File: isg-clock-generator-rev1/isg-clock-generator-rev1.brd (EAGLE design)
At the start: 76.2 x 50.8 mm, 68 parts, among them IC1 LMK03318RHSR, X1 OUT0_P, X2 OUT0_N, X3 OUT1_P, X4 OUT1_N

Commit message: More progress idk
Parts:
- removed JP1: (no value), jumper:JP5Q
- added C44, C45, C49, C50: CAP CER 10000PF 25V X7R 0603 10%, rcl-modified-footprints:C0603
- added C46, C48, C51, C53: CAP CER 0.1UF 25V X7R 0603 10%, rcl-modified-footprints:C0603
- added C47, C52: CAP CER 10UF 16V X7R 0805 20%, rcl:C0805
- added C54: CAP CER 0.01uF X7R 0402, rcl-modified-footprints:C0402
- added C55: CAP CER 22uF 6.3V 0603, rcl-modified-footprints:C0603
- added C56: CAP CER 0.033uF 0603, rcl-modified-footprints:C0603
- added C57: CAP CER 3300pF 0603, rcl-modified-footprints:C0603
- added C58, C62, C63: DNP, rcl-modified-footprints:C0603
- added C59, C60: 0R JUMPER, rcl-modified-footprints:C0603
- added C61: DNP, rcl-modified-footprints:C0402
- added IC2, IC3: TPS7A4901, Kramnik's Library:MSOP-8_POWER_PAD
- added JP10: RSEL, isg-clock-generator:JP2_ROUND
- added JP11: (no value), jumper:JP8Q
- added JP12: (no value), jumper:JP3Q
- added JP13: PRIREF_VCM, jumper:JP2
- added JP14: CON_OST_302-S101, Kramnik's Library:CON_OST_302-S101
- added JP2: STAT_LED_EN, jumper:JP1
- added JP3: GPIO5, isg-clock-generator:JP2_ROUND
- added JP4: GPIO4, isg-clock-generator:JP2_ROUND
- added JP5: GPIO3, isg-clock-generator:JP2_ROUND
- added JP6: GPIO2, isg-clock-generator:JP2_ROUND
- added JP7: GPIO1, isg-clock-generator:JP2_ROUND
- added JP8: GPIO0, isg-clock-generator:JP2_ROUND
- added JP9: HWCTRL, isg-clock-generator:JP2_ROUND
- added R10, R14: RES SMD 76.8K OHM 1% 1/10W 0603, rcl-modified-footprints:R0603
- added R11, R12, R13, R26, R28, R29, R41, R42, R44, R45, R49, R50, R51, R52, R53, R6, R8, R9: DNP, rcl-modified-footprints:R0603
- added R15, R17, R18, R7: RES SMD 24K OHM 1% 1/10W 0603, rcl-modified-footprints:R0603
- added R16, R27, R30, R33, R36, R40, R43: RES SMD 1K OHM 1% 1/10W 0603, rcl-modified-footprints:R0603
- added R19: RES SMD 0 OHM 1% 1/10W 0603, rcl-modified-footprints:R0603
- added R20: RES SMD 2.32K OHM 1% 1/10W 0603, rcl-modified-footprints:R0603
- added R21: RES SMD 5.62K OHM 1% 1/10W 0603, rcl-modified-footprints:R0603
- added R22: RES SMD 10.5K OHM 1% 1/10W 0603, rcl-modified-footprints:R0603
- added R23: RES SMD 18.7K OHM 1% 1/10W 0603, rcl-modified-footprints:R0603
- added R24: RES SMD 34.8K OHM 1% 1/10W 0603, rcl-modified-footprints:R0603
- added R25: RES SMD 84.5K OHM 1% 1/10W 0603, rcl-modified-footprints:R0603
- added R3, R4, R46, R47, R48, R5: 0R JUMPER 0603, rcl-modified-footprints:R0603
- added R31, R34, R37, R39: RES SMD 13.0K OHM 1% 1/10W 0603, rcl-modified-footprints:R0603
- added R32, R35, R38: RES SMD 4.99K OHM 1% 1/10W 0603, rcl-modified-footprints:R0603
- added X5: OUT1_P, con-coax:J502-ND-142-0701-881/886
- Q1: value (none) -> 7M50072001
- R1, R2: value 510 -> RES SMD 510R 0603
- X3: value OUT1_P -> OUT2_P
- X4: value OUT1_N -> OUT1_P
- moved LED1 95.0 mm to (19.7, 43.8), turned to 270 degrees
- moved LED2 93.5 mm to (19.7, 40.3), turned to 270 degrees
- moved X4 89.4 mm to (47.6, 61.9), turned to 270 degrees
- moved X3 42.7 mm to (19.1, 1.59), turned to 90 degrees
- moved X2 40.9 mm to (38.1, 1.59), turned to 90 degrees
- moved X1 38.9 mm to (57.1, 1.59), turned to 90 degrees
- moved Q1 25.7 mm to (34.3, 44.5), turned to 270 degrees
- moved C7 13.1 mm to (29.2, 29.2), turned to 270 degrees
- moved C1 12.7 mm to (36.8, 35.6), turned to 90 degrees
- moved H3 12.7 mm to (72.4, 59.7)
- moved H4 12.7 mm to (3.81, 59.7)
- moved C2 5.24 mm to (47.0, 27.9)
- moved C3 5.24 mm to (47.0, 24.1)
- moved IC1 2.84 mm to (38.1, 25.4)
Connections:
- net LF2 renamed NC_PIN
- net N$17 renamed STATUS0
- net N$18 renamed STATUS1
- removed net N$15: IC1.10
- removed net N$16: IC1.7
- removed net N$19: IC1.6
- removed net NC_OUT2_P: IC1.20
- removed net OUT1_N: IC1.16, X4.1
- removed net OUT1_P: IC1.17, X3.1
- new net GPIO5_SEL_11_12: JP11.12, R24.2
- new net GPIO5_SEL_13_14: JP11.14, R25.2
- new net GPIO5_SEL_15_16: JP11.16, R26.2
- new net GPIO5_SEL_1_2: JP11.2, R19.2
- new net GPIO5_SEL_3_4: JP11.4, R20.2
- new net GPIO5_SEL_5_6: JP11.6, R21.2
- new net GPIO5_SEL_7_8: JP11.8, R22.2
- new net GPIO5_SEL_9_10: JP11.10, R23.2
- new net LDO_P3V3_SS: C44.1, C49.1, IC2.6, IC3.6
- new net LDO_P5V0_FB_CH1: C45.2, C50.2, IC2.2, IC3.2, R10.1, R14.1, R15.1, R7.1
- new net N$1: R6.2, R8.2, R9.2
- new net N$10: JP14.3
- new net N$11: JP14.1
- new net N$12: JP14.8
- new net N$13: JP14.4
- new net N$22: C55.1, JP12.5
- new net N$23: C56.1, JP12.3
- new net N$24: JP4.2, R27.1
- new net N$25: JP5.2, R30.1
- new net N$26: JP8.2, R39.1
- new net N$27: JP6.2, R33.1
- new net N$28: JP9.2, R40.1
- new net N$29: JP7.2, R36.1
- new net N$30: C57.1, JP12.1
- new net N$31: JP10.2, R43.1
- new net N$32: JP12.2, JP12.4, JP12.6, R46.2
- new net N$4: JP3.3, R16.1
- new net N$5: JP13.3, R51.1, R52.2
- new net N$6: JP14.5, R53.1
- new net NC_OUT1_N: IC1.16
- new net NC_OUT1_P: IC1.17
- new net OUT0_R_N: R12.2, R4.1, R8.1, X2.1
- new net OUT0_R_P: R11.2, R3.1, R6.1, X1.1
- new net OUT2_P: IC1.20, R5.2
- new net OUT2_R_P: R13.2, R5.1, R9.1, X3.1
- new net PP_P1V8_VDDO: C26.1, C30.1, C34.1, C38.1, C42.1, C45.1, C46.1, C47.1, C6.1, IC2.1, L1.2, L10.2, L6.2, L7.2, L8.2, L9.2, R10.2
- new net PP_P3V3_PLL_CORE: C20.1, C21.1, C22.1, C23.1, C50.1, C51.1, C52.1, IC3.1, JP10.3, JP2.2, JP4.3, JP5.3, JP6.3, JP7.3, JP8.3, JP9.3, L2.1, L3.1, L4.1, L5.1, R14.2, R16.2, R17.1, R28.2, R31.2, R34.2, R37.2, R41.2, R44.2, R51.2, R53.2
- new net PRIREF_N: IC1.7, R48.1, R50.2
- new net PRIREF_P: IC1.6, R47.1, R49.2
- new net PRIREF_RC_N: C60.1, X5.1
- new net PRIREF_RC_P: C59.1, X4.1
- new net PRIREF_R_N: C60.2, R48.2
- new net PRIREF_R_P: C59.2, R47.2
- new net PRIREF_VCM: C61.1, JP13.2, R49.1, R50.1
- new net SECREF_N: C62.1, IC1.11, Q1.1
- new net SECREF_P: C63.1, IC1.10, Q1.3
- new net STATUS_LED_PWR: JP2.1, R1.2, R2.2
- new net VIN: C48.1, C53.1, IC2.8, IC3.8, R18.1
- net GND: now also C44.2, C46.2, C47.2, C48.2, C49.2, C51.2, C52.2, C53.2, C54.2, C55.2, C56.2, C57.2, C58.2, C61.2, C62.2, C63.2, IC2.4, IC2.PAD, IC3.4, IC3.PAD, JP10.1, JP11.1, JP11.11, JP11.13, JP11.15, JP11.3, JP11.5, JP11.7, JP11.9, JP13.1, JP14.6, JP3.1, JP4.1, JP5.1, JP6.1, JP7.1, JP8.1, JP9.1, R11.1, R12.1, R13.1, R15.2, R29.1, R32.1, R35.1, R38.1, R42.1, R45.1, R52.1, R7.2, X5.G@1, X5.G@2, X5.G@3, X5.G@4
- net GPIO0: now also R39.2
- net GPIO1: now also R36.2, R37.1, R38.2
- net GPIO2: now also R33.2, R34.1, R35.2
- net GPIO3: now also R30.2, R31.1, R32.2
- net GPIO4: now also R27.2, R28.1, R29.2
- net GPIO5: now also JP3.2, R19.1, R20.1, R21.1, R22.1, R23.1, R24.1, R25.1, R26.1
- net HW_SW_CTRL: now also R40.2, R41.1, R42.2
- net LF1: now also C58.1, R46.1
- net N$14: now also JP14.2; no longer IC1.11
- net N$2: now also IC2.5, R17.2; no longer C20.1, C21.1, C22.1, C23.1, L2.1, L3.1, L4.1, L5.1
- net N$3: now also IC3.5, R18.2; no longer C26.1, C30.1, C34.1, C38.1, C42.1, C6.1, L1.2, L10.2, L6.2, L7.2, L8.2, L9.2
- net N$9: now also JP14.7; no longer R1.2, R2.2
- net OUT0_N: now also R4.2; no longer X2.1
- net OUT0_P: now also R3.2; no longer X1.1
- net PDN: now also C54.1
- net REFSEL: now also R43.2, R44.1, R45.2
- net SCL: now also JP14.9
- net SDA: now also JP14.10
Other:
- board size 76.2 x 50.8 mm -> 76.2 x 63.5 mm
- board text added: "1GHz PLL Clock Source kramnik@berkeley.edu"

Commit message: Started decap placement
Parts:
- IC1: device isg-clock-generator:RHS0048A -> isg-clock-generator:RHS0048A_NV
- X4: value OUT1_P -> PRIREF_P
- X5: value OUT1_P -> PRIREF_N
- moved C40 302.4 mm to (39.1, 17.5), turned to 270 degrees
- moved C43 299.6 mm to (39.1, 19.7), turned to 270 degrees
- moved C41 296.1 mm to (39.1, 21.3), flipped to the bottom, turned to 90 degrees
- moved C36 293.3 mm to (41.0, 33.3), turned to 90 degrees
- moved C39 286.1 mm to (41.0, 31.1), turned to 90 degrees
- moved C37 279.6 mm to (41.0, 29.5), flipped to the bottom, turned to 270 degrees
- moved C32 268.1 mm to (39.4, 33.3), turned to 90 degrees
- moved C35 260.9 mm to (39.4, 31.1), turned to 90 degrees
- moved C33 254.4 mm to (39.4, 29.5), flipped to the bottom, turned to 270 degrees
- moved C28 242.8 mm to (37.8, 33.3), turned to 90 degrees
- moved C31 235.7 mm to (37.8, 31.1), turned to 90 degrees
- moved C29 229.2 mm to (37.8, 29.5), flipped to the bottom, turned to 270 degrees
- moved C24 217.7 mm to (36.2, 33.3), turned to 90 degrees
- moved C27 210.6 mm to (36.2, 31.1), turned to 90 degrees
- moved C25 204.1 mm to (36.2, 29.5), flipped to the bottom, turned to 270 degrees
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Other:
- board text added: "1GHz PLL Clock Source kramnik@berkeley.edu vlada@berkeley.edu"
- board text removed: "1GHz PLL Clock Source kramnik@berkeley.edu"

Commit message: Fit all components on board except power supplies (need to swap LDO part)
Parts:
- JP13: device jumper:JP2 -> isg-clock-generator:JP2_ROUND
- moved C52 437.5 mm to (52.4, 99.4)
- moved R52 424.4 mm to (23.8, 60.0)
- moved R53 419.6 mm to (5.40, 56.2)
- moved R51 419.2 mm to (20.6, 60.0)
- moved R12 338.9 mm to (54.6, 8.57)
- moved R13 338.2 mm to (16.2, 9.21)
- moved R11 331.1 mm to (35.2, 8.57), turned to 180 degrees
- moved R8 327.2 mm to (59.4, 8.89)
- moved R9 325.2 mm to (21.6, 8.89)
- moved R6 318.4 mm to (40.0, 8.26)
- moved C38 303.3 mm to (41.0, 38.4), turned to 90 degrees
- moved C42 302.4 mm to (39.1, 12.4), turned to 270 degrees
- moved L10 284.9 mm to (39.1, 14.9), turned to 270 degrees
- moved L9 280.8 mm to (41.0, 35.9), turned to 90 degrees
- moved C34 278.0 mm to (39.4, 38.4), turned to 90 degrees
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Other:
- board size 76.2 x 63.5 mm -> 76.2 x 76.2 mm

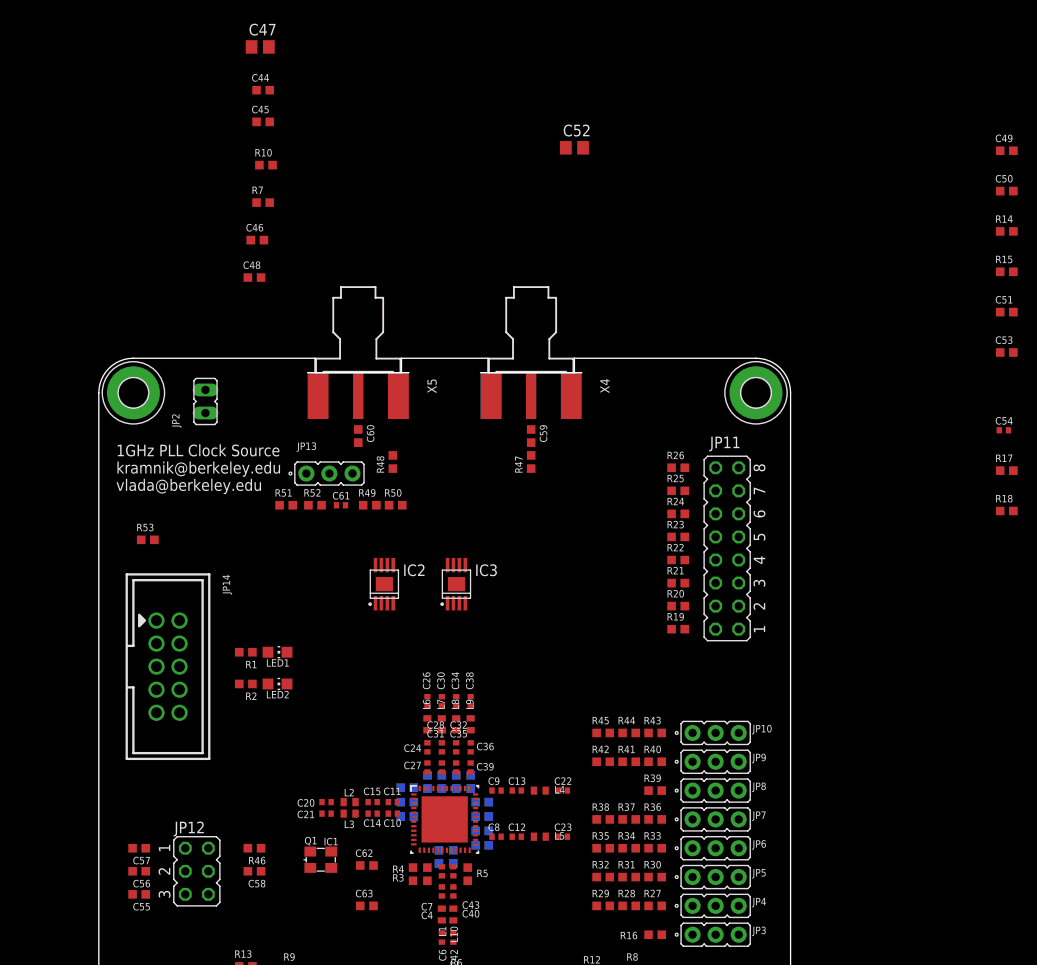
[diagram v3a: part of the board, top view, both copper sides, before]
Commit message: Updated LDOs for 1A, all parts roughly placed in layout, power input TODO
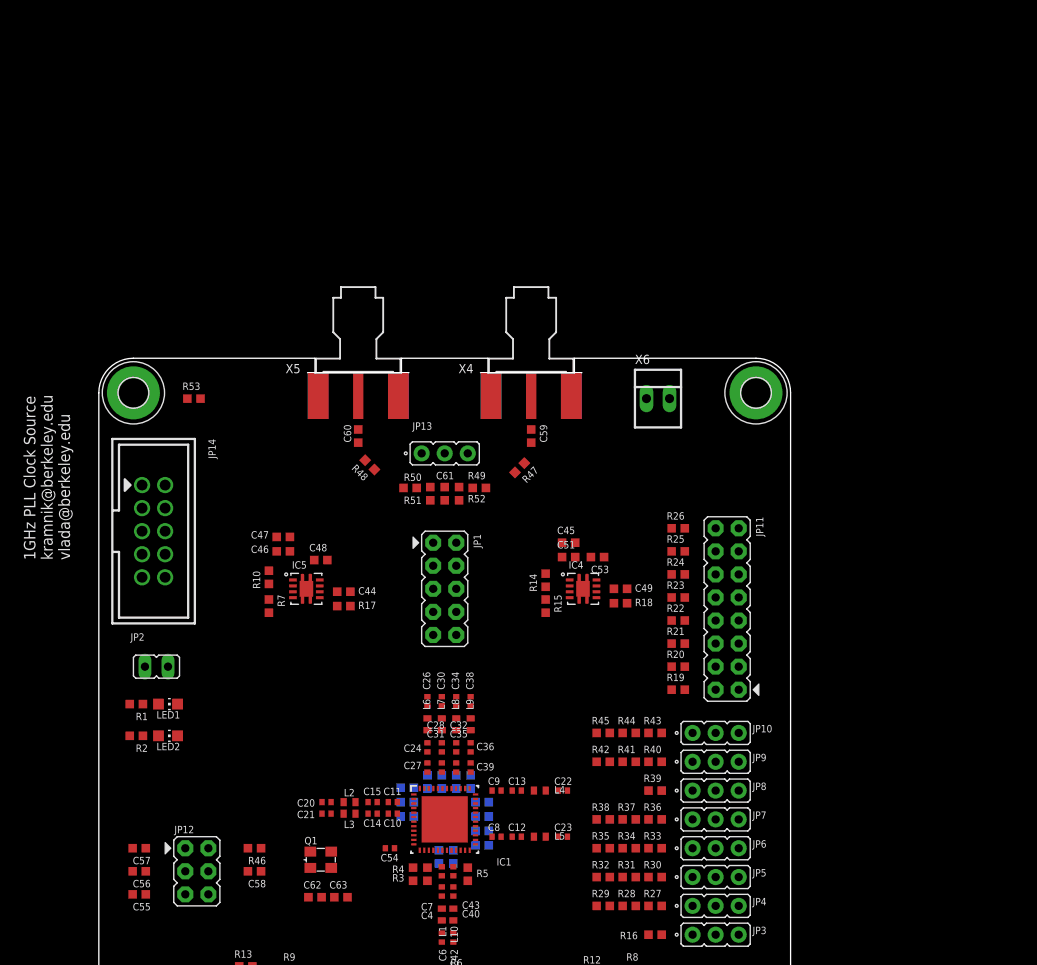
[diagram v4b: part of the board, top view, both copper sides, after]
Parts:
- removed C50: CAP CER 10000PF 25V X7R 0603 10%, rcl-modified-footprints:C0603
- removed C52: CAP CER 10UF 16V X7R 0805 20%, rcl:C0805
- removed IC2, IC3: TPS7A4901, Kramnik's Library:MSOP-8_POWER_PAD
- added IC4, IC5: TPS7A8001DRBR, isg-clock-generator:DRB8_1P75X1P5
- added JP1: MOTHERBOARD, isg-clock-generator:JP5Q
- added X6: 22-23-2021, con-molex:22-23-2021
- C45: value CAP CER 10000PF 25V X7R 0603 10% -> CAP CER 4.7UF 6.3V X5R 0603 10%
- C47: value CAP CER 10UF 16V X7R 0805 20% -> CAP CER 4.7UF 6.3V X5R 0603 10%; device rcl:C0805 -> rcl-modified-footprints:C0603
- C61: value DNP -> DNP 0603; device rcl-modified-footprints:C0402 -> rcl-modified-footprints:C0603
- JP11: value (none) -> XO_MARGIN; device jumper:JP8Q -> isg-clock-generator:JP8Q
- JP12: value (none) -> LOOP_FILTER; device jumper:JP3Q -> isg-clock-generator:JP3Q
- R10, R14: value RES SMD 76.8K OHM 1% 1/10W 0603 -> RES SMD 4.99K OHM 1% 1/10W 0603
- R15: value RES SMD 24K OHM 1% 1/10W 0603 -> RES SMD 1.62K OHM 1% 1/10W 0603
- R17, R18: value RES SMD 24K OHM 1% 1/10W 0603 -> RES SMD 4.99K OHM 1% 1/10W 0603
- R51, R52: value DNP -> DNP 0603
- R7: value RES SMD 24K OHM 1% 1/10W 0603 -> RES SMD 3.92K OHM 1% 1/10W 0603
- moved C54 81.8 mm to (32.1, 22.2), turned to 180 degrees
- moved R17 74.5 mm to (27.0, 48.9), turned to 180 degrees
- moved C49 64.3 mm to (57.5, 50.8)
- moved R14 63.7 mm to (49.2, 51.8), turned to 90 degrees
- moved R15 62.7 mm to (49.2, 48.9), turned to 270 degrees
- moved C45 57.3 mm to (51.8, 55.9)
- moved C44 56.0 mm to (27.0, 50.5)
- moved C51 55.3 mm to (51.8, 54.3)
- moved C47 54.0 mm to (20.3, 56.5)
- moved C53 50.4 mm to (54.9, 54.3), turned to 180 degrees
- moved R10 45.4 mm to (18.7, 52.1), turned to 90 degrees
- moved R7 44.5 mm to (18.7, 48.9), turned to 270 degrees
- moved R18 43.7 mm to (57.5, 49.2), turned to 180 degrees
- moved C46 34.4 mm to (20.3, 54.9)
- moved C48 32.0 mm to (24.4, 54.0)
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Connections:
- net N$22 renamed LF_NARROW
- net N$23 renamed LF_FRAC_N
- net N$30 renamed LF_INT_N\
- net N$32 renamed LF_R
- removed net LDO_P3V3_SS: C44.1, C49.1, IC2.6, IC3.6
- removed net LDO_P5V0_FB_CH1: C45.2, C50.2, IC2.2, IC3.2, R10.1, R14.1, R15.1, R7.1
- removed net N$2: IC2.5, R17.2
- removed net N$3: IC3.5, R18.2
- new net LDO_PVCORE_EN: IC4.5, R18.2
- new net LDO_PVCORE_FB: IC4.3, R14.1, R15.1
- new net LDO_PVCORE_SS: C49.1, IC4.6
- new net LDO_PVDDIO_EN: IC5.5, R17.2
- new net LDO_PVDDIO_FB: IC5.3, R10.1, R7.1
- new net LDO_PVDDIO_SS: C44.1, IC5.6
- net GND: now also C45.2, IC4.4, IC4.9, IC5.4, IC5.9; no longer C52.2, IC2.4, IC2.PAD, IC3.4, IC3.PAD
- net PP_P1V8_VDDO: now also IC5.1, IC5.2; no longer C45.1, IC2.1
- net PP_P3V3_PLL_CORE: now also C45.1, IC4.1, IC4.2; no longer C50.1, C52.1, IC3.1
- net VIN: now also IC4.7, IC4.8, IC5.7, IC5.8; no longer IC2.8, IC3.8
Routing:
- added copper zone on layer 2, net GND

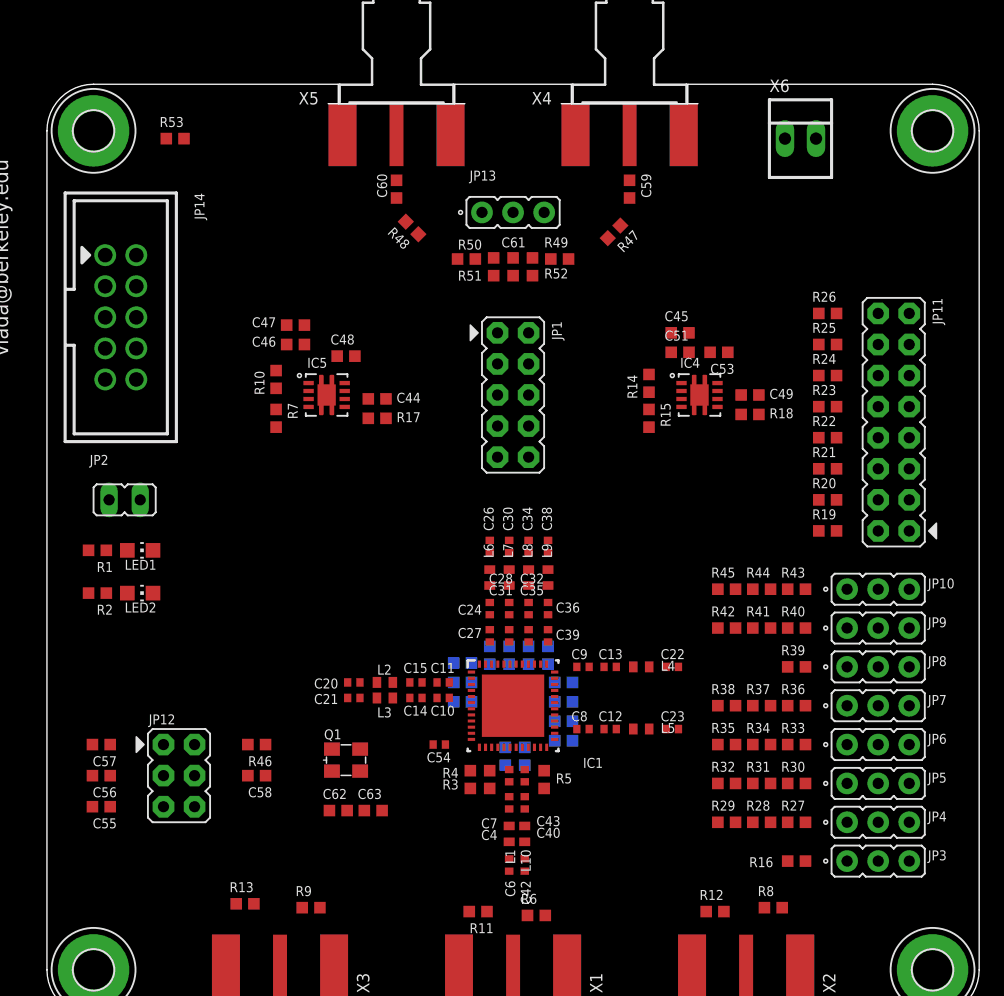
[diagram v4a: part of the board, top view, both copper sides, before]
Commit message: Started working on routing
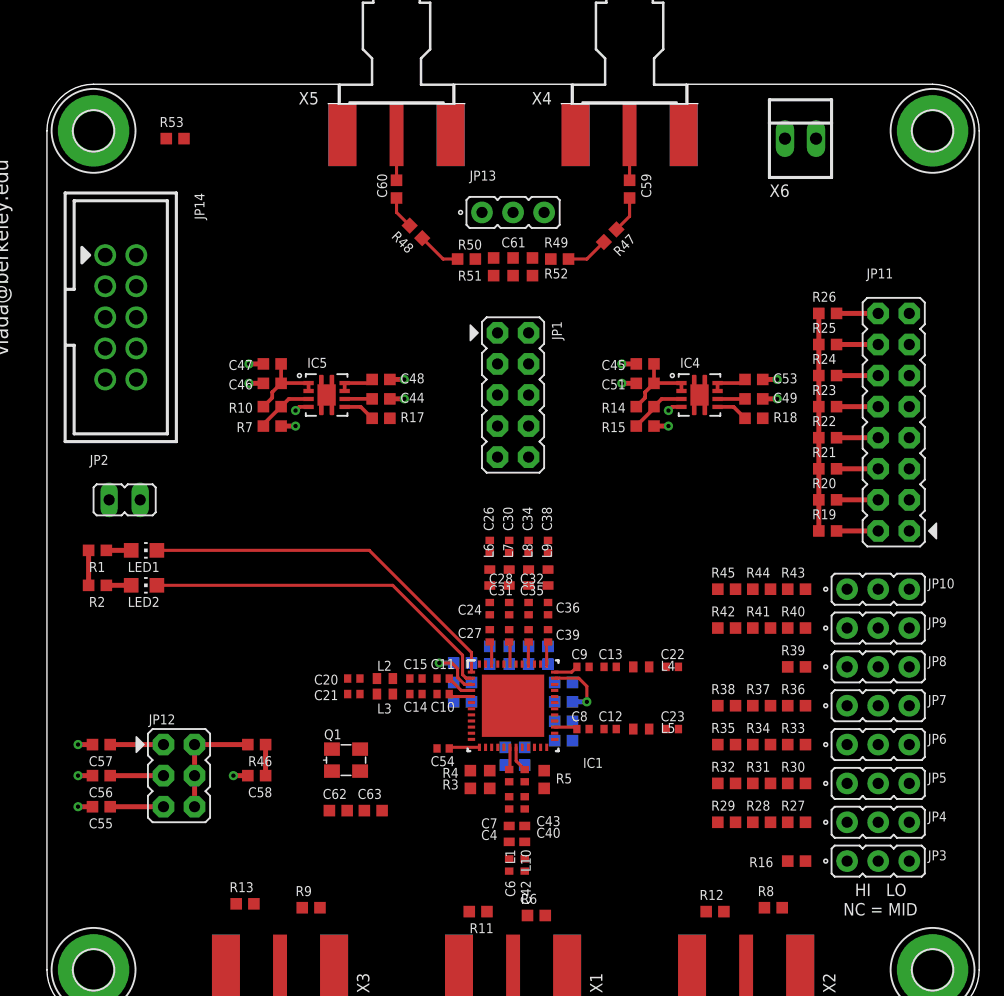
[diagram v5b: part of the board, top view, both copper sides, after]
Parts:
- JP10: value RSEL -> REFSEL
- R40: value RES SMD 1K OHM 1% 1/10W 0603 -> RES SMD 10K OHM 1% 1/10W 0603
- X6: value 22-23-2021 -> V_INPUT
- moved C45 3.82 mm to (48.9, 53.3), turned to 180 degrees
- moved C51 3.82 mm to (48.9, 51.8), turned to 180 degrees
- moved C46 3.70 mm to (18.4, 51.8), turned to 180 degrees
- moved C47 3.70 mm to (18.4, 53.3), turned to 180 degrees
- moved C53 3.62 mm to (57.8, 52.1), turned to 0 degrees
- moved C48 3.43 mm to (27.3, 52.1)
- moved R10 2.25 mm to (18.4, 49.8), turned to 180 degrees
- moved R14 1.93 mm to (48.9, 49.8), turned to 180 degrees
- moved R7 0.71 mm to (18.4, 48.3), turned to 0 degrees
- moved R15 0.71 mm to (48.9, 48.3), turned to 0 degrees
- moved LED2 0.71 mm to (7.94, 35.2)
- moved R2 0.63 mm to (4.13, 35.2)
- moved C54 0.45 mm to (32.4, 21.9)
- moved R47 0.45 mm to (46.0, 63.8)
- moved R48 0.45 mm to (30.2, 64.1)
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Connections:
- net GND: now also JP1.3, JP1.4, JP1.6
- net HW_SW_CTRL: now also JP1.8
- net SCL: now also JP1.10
- net SDA: now also JP1.9
- net STATUS0: now also JP1.7
- net STATUS1: now also JP1.5
- net VIN: now also JP1.1, JP1.2
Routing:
- net STATUS0: track 0.00 -> 30.8 mm
- net STATUS1: track 0.00 -> 29.8 mm
- net GND: track 0.00 -> 18.9 mm, vias 0 -> 16
- net GPIO5: track 0.00 -> 17.8 mm
- net LF_R: track 0.00 -> 9.44 mm
- net PP_P1V8_VDDO: track 0.00 -> 7.00 mm
- net PP_P3V3_PLL_CORE: track 0.00 -> 6.98 mm
- net VIN: track 0.00 -> 6.03 mm
- net DECAP_PLL: track 0.00 -> 5.36 mm, vias 0 -> 1
- net DECAP_DIG: track 0.00 -> 4.95 mm, vias 0 -> 1
- net LDO_PVDDIO_FB: track 0.00 -> 4.69 mm
- net LDO_PVCORE_FB: track 0.00 -> 4.69 mm
- net LF_NARROW: track 0.00 -> 4.36 mm
- net LF_INT_N\: track 0.00 -> 4.36 mm
- net LF_FRAC_N: track 0.00 -> 4.36 mm
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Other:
- board text added: "HI"
- board text added: "LO"
- board text added: "NC = MID"
